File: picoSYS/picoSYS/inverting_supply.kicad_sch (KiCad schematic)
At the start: 17 parts, among them U1 MC34063AP

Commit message: reading info
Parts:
- R1: value 10R -> 0R
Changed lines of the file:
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@@
 			)
 		)
-		(property "Value" "10R"
+		(property "Value" "0R"
 			(at 29.718 25.3421 0)
 			(effects

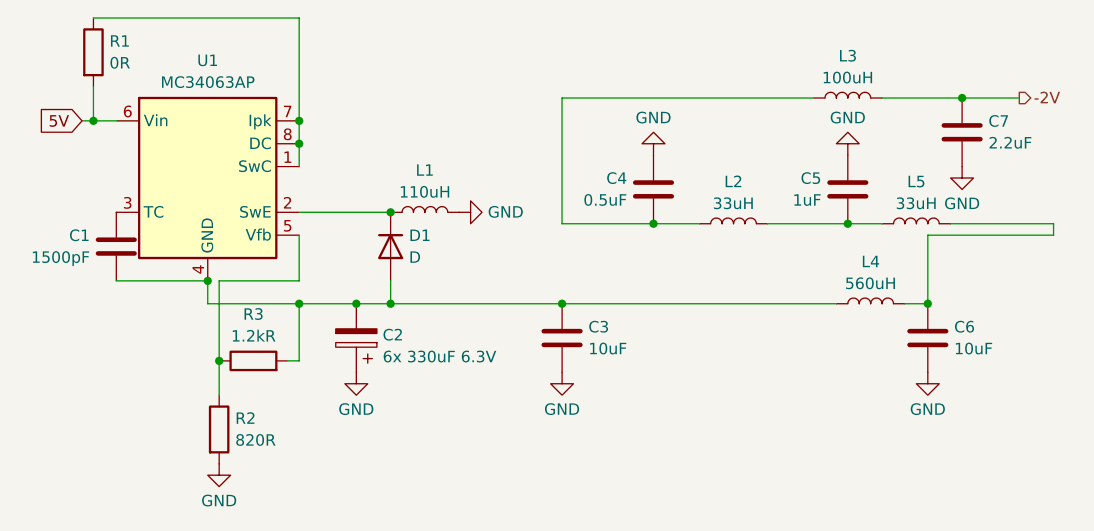
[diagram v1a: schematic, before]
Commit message: updated schematic to better reflect real hardware, removed a debug message
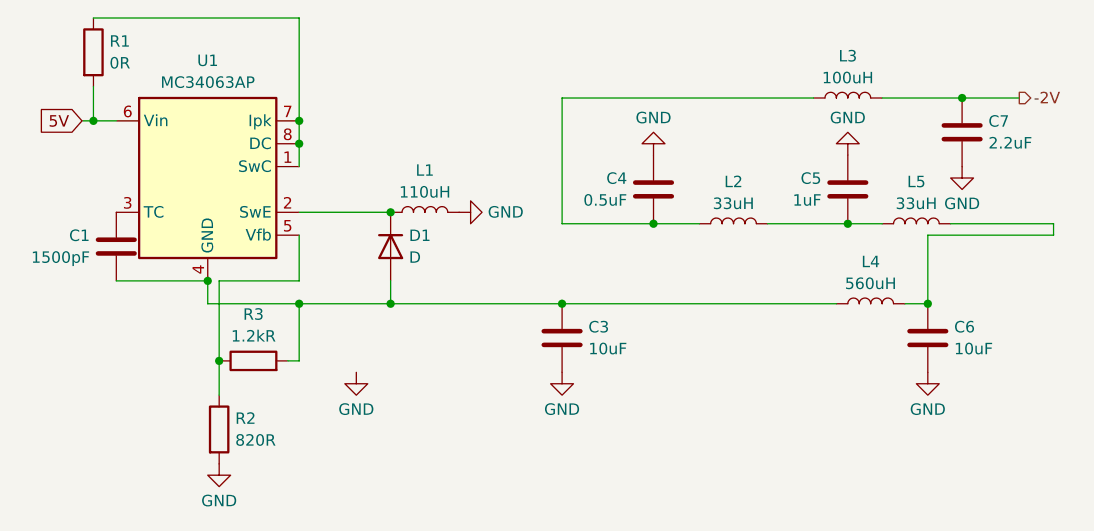
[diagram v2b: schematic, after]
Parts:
- removed C2: 6x 330uF 6.3V, symbol Device:C_Polarized
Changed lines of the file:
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@@
-	)
-	(junction
-		(at 57.15 52.07)
-		(diameter 0)
-		(color 0 0 0 0)
 	)
 	(junction
@@
 	(wire
 		(pts
-			(xy 57.15 52.07) (xy 60.96 52.07)
-		)
-		(stroke
-			(width 0)
-			(type default)
-		)
-	)
-	(wire
-		(pts
 			(xy 41.91 58.42) (xy 41.91 62.23)
 		)
@@
 	(wire
 		(pts
-			(xy 50.8 52.07) (xy 57.15 52.07)
+			(xy 50.8 52.07) (xy 60.96 52.07)
 		)
 		(stroke
@@
 					(unit 1)
 				)
-			)
-		)
-	)
-	(symbol
-		(lib_id "Device:C_Polarized")
-		(at 57.15 55.88 180)
-		(unit 1)
-		(exclude_from_sim no)
-		(in_bom yes)
-		(on_board yes)
-		(dnp no)
-		(property "Reference" "C2"
-			(at 60.071 55.5568 0)
-			(effects
-				(font
-					(size 1.27 1.27)
-				)
-				(justify right)
-			)
-		)
-		(property "Value" "6x 330uF 6.3V"
-			(at 60.071 57.9811 0)
-			(effects
-				(font
-					(size 1.27 1.27)
-				)
-				(justify right)
-			)
-		)
-		(property "Footprint" ""
-			(at 56.1848 52.07 0)
-			(effects
-				(font
-					(size 1.27 1.27)
-				)
-				(hide yes)
-			)
-		)
-		(property "Datasheet" "~"
-			(at 57.15 55.88 0)
-			(effects
-				(font
-					(size 1.27 1.27)
-				)
-				(hide yes)
-			)
-		)
-		(property "Description" "Polarized capacitor"
-			(at 57.15 55.88 0)
-			(effects
-				(font
-					(size 1.27 1.27)
-				)
-				(hide yes)
-			)
-		)
-		(pin "2"
-		)
-		(pin "1"
-		)
-		(instances
-			(project "picoSYS"
-				(path "/c5b94243-0015-46aa-9508-ff5973f88339/d2b00318-2e60-4c8a-9afb-1b2401ad5490"
-					(reference "C2")
-					(unit 1)
-				)
